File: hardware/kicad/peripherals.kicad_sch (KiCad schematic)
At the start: 28 parts, among them J301 IT8951 HAT, SW301 PEC11R-4215F-S0024, SW302 POWER, U301 CAP1188-1-CP-TR

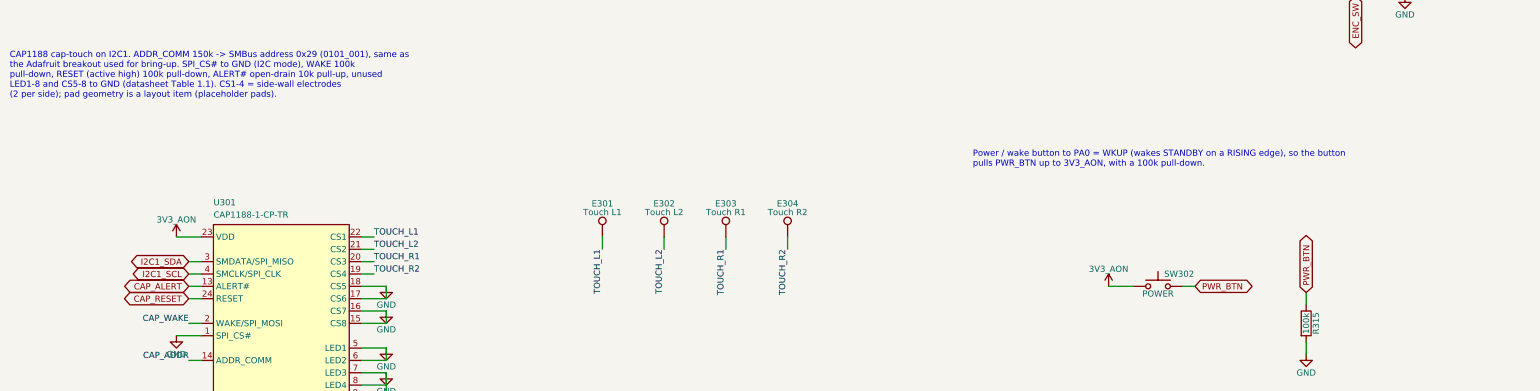
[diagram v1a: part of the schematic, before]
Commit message: Apply enclosure decisions: bottom-edge power button, electrode boards, leaded NTC
Decisions (2026-09-23): keep the HAT's 2x20 header for v1; move the power
button to the bottom edge; put the side-wall electrodes on two small
boards; keep the front-face knob; put RT1 on leads to the cell.

Schematic (via the generator scripts, check_schematic.py passes):
- SW302: Alps SKRTLAE010 side-actuated switch on the PCB's bottom edge.
- E301-E304 test pads -> J302/J303 JST-SH 3-pin (touch / GND / touch),
  cabled to the electrode boards.
- RT1: leaded Murata NXFT15XH103FA2B (same 10k/B3380 curve) on solder
  pads, head taped to the pouch.

Enclosure: flexure tab in the bottom wall over the switch; two identical
74 x 10 mm electrode boards in printed channels on the side walls; PCB
and battery 2.5 mm in from the walls to make room; new checks for the
button travel and electrode coverage (21 pass, no interferences);
electrode_board.json export and a bottom-edge render.

Co-Authored-By: Claude Opus 5.5 <noreply@anthropic.com>
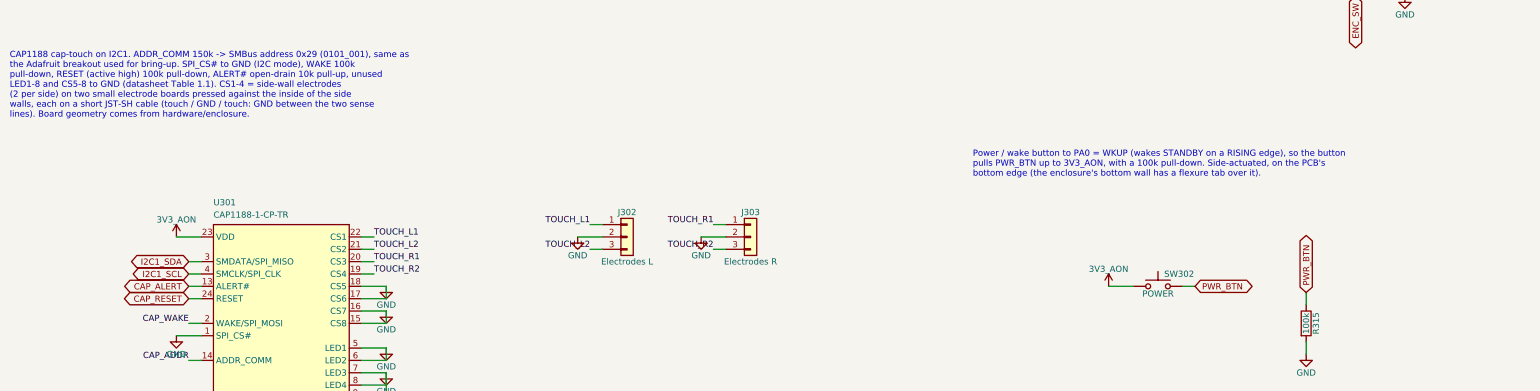
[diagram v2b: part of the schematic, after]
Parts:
- removed E302: Touch L2, TestPoint:TestPoint_Pad_4.0x4.0mm, symbol Connector:TestPoint
- removed E303: Touch R1, TestPoint:TestPoint_Pad_4.0x4.0mm, symbol Connector:TestPoint
- removed E304: Touch R2, TestPoint:TestPoint_Pad_4.0x4.0mm, symbol Connector:TestPoint
- added J303: Electrodes R, Connector_JST:JST_SH_SM03B-SRSS-TB_1x03-1MP_P1.00mm_Horizontal, symbol Connector_Generic:Conn_01x03
- J302: renamed from E301; value Touch L1 -> Electrodes L; footprint TestPoint:TestPoint_Pad_4.0x4.0mm -> Connector_JST:JST_SH_SM03B-SRSS-TB_1x03-1MP_P1.00mm_Horizontal; symbol Connector:TestPoint -> Connector_Generic:Conn_01x03; MPN (none) -> SM03B-SRSS-TB
- SW302: footprint Button_Switch_SMD:SW_Push_1P1T_NO_CK_KMR2 -> Button_Switch_SMD:SW_Push_1P1T-MP_NO_Horizontal_Alps_SKRTLAE010; MPN (none) -> SKRTLAE010
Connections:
- net GND: now also J302.2 (Pin_2), J303.2 (Pin_2)
- net TOUCH_L2: now also J302.3 (Pin_3)
- net TOUCH_R1: now also J303.1 (Pin_1)
- net TOUCH_R2: now also J303.3 (Pin_3)
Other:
- note added: "CAP1188 cap-touch on I2C1. ADDR_COMM 150k -> SMBus address 0x29 (0101_001), same as the Adafruit breakout used for bring-up. SPI_CS# to GND (I2C mode), WAKE 100k pull-down, RESET (active high) 100k pull-down, ALERT# open-drain 10k pull-up, unused LED1-8 and CS5-8 to GND (datasheet Table 1.1). CS1-4 = side-wall electrodes (2 per side) on two small electrode boards pressed against the inside of the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"
- note added: "Power / wake button to PA0 = WKUP (wakes STANDBY on a RISING edge), so the button pulls PWR_BTN up to 3V3_AON, with a 100k pull-down. Side-actuated, on the PCB's bottom edge (the enclosure's bottom wall has a flexure tab over it)."
- note removed: "CAP1188 cap-touch on I2C1. ADDR_COMM 150k -> SMBus address 0x29 (0101_001), same as the Adafruit breakout used for bring-up. SPI_CS# to GND (I2C mode), WAKE 100k pull-down, RESET (active high) 100k pull-down, ALERT# open-drain 10k pull-up, unused LED1-8 and CS5-8 to GND (datasheet Table 1.1). CS1-4 = side-wall electrodes (2 per side); pad geometry is a layout item (placeholder pads)."
- note removed: "Power / wake button to PA0 = WKUP (wakes STANDBY on a RISING edge), so the button pulls PWR_BTN up to 3V3_AON, with a 100k pull-down."

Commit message: Electrode board project, open hardware TODOs, main PCB bootstrap
- hardware/electrode/: side-wall electrode board (one design, two fitted),
  generated by gen_electrode.py (schematic, pad footprint) and
  gen_electrode_pcb.py (board, via KiCad's pcbnew Python) from the
  enclosure's params.py. ERC/DRC/parity clean.
- Datasheet values replace most enclosure placeholders. The encoder is now
  PEC11R-4220F-S0024 (20 mm shaft): the M7 bushing left the 15 mm shaft
  too short for the knob. Knob redesigned around the bushing.
- Schematic: TPD4E05U06 ESD on the electrode lines, HRDY 100k pull-down,
  crystals chosen (NX3225GD 8 MHz / NX3215SA 32.768 kHz) with recomputed
  load caps, all inductors DFE201612E, M2 mounting holes.
- Decisions recorded: USB shield to GND, UVLO restart analysis, soft power
  = STANDBY + WKUP, no fuel gauge on v1, TPS63900 footprint verified.
- Encoder footprint: silkscreen no longer crosses its own lug pads.
- hardware/kicad/stm32-epaper.kicad_pcb: 4-layer board bootstrapped by
  gen_main_pcb.py with the enclosure outline, all footprints and nets, and
  the enclosure-fixed parts placed.

Co-Authored-By: Claude Opus 5.5 <noreply@anthropic.com>
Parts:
- added H301, H302, H303, H304: M2, MountingHole:MountingHole_2.2mm_M2, symbol Mechanical:MountingHole
- added U301: CAP1188-1-CP-TR, Package_DFN_QFN:QFN-24-1EP_4x4mm_P0.5mm_EP2.5x2.5mm, symbol epaper:CAP1188
- added U302: TPD4E05U06DQAR, Package_SON:USON-10_2.5x1.0mm_P0.5mm, symbol Power_Protection:TPD4E05U06DQA
- R316: renamed from U301; value CAP1188-1-CP-TR -> 100k; footprint Package_DFN_QFN:QFN-24-1EP_4x4mm_P0.5mm_EP2.5x2.5mm -> Resistor_SMD:R_0402_1005Metric; symbol epaper:CAP1188 -> Device:R; MPN CAP1188-1-CP-TR -> (none)
- SW301: value PEC11R-4215F-S0024 -> PEC11R-4220F-S0024; MPN PEC11R-4215F-S0024 -> PEC11R-4220F-S0024
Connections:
- net 3V3_AON: now also U301.23 (VDD); no longer R316.23 (VDD)
- net CAP_ADDR: now also U301.14 (ADDR_COMM); no longer R316.14 (ADDR_COMM)
- net CAP_ALERT: now also U301.13 (ALERT#); no longer R316.13 (ALERT#)
- net CAP_RESET: now also U301.24 (RESET); no longer R316.24 (RESET)
- net CAP_WAKE: now also U301.2 (WAKE/SPI_MOSI); no longer R316.2 (WAKE/SPI_MOSI)
- net EPD_HRDY: now also R316.1
- net GND: now also R316.2, U301.1 (SPI_CS#), U301.10 (LED6), U301.11 (LED7), U301.12 (LED8), U301.15 (CS8), U301.16 (CS7), U301.17 (CS6), U301.18 (CS5), U301.25 (GND), U301.5 (LED1), U301.6 (LED2), U301.7 (LED3), U301.8 (LED4), U301.9 (LED5), U302.3 (GND), U302.8 (GND); no longer R316.1 (SPI_CS#), R316.10 (LED6), R316.11 (LED7), R316.12 (LED8), R316.15 (CS8), R316.16 (CS7), R316.17 (CS6), R316.18 (CS5), R316.25 (GND), R316.5 (LED1), R316.6 (LED2), R316.7 (LED3), R316.8 (LED4), R316.9 (LED5)
- net I2C1_SCL: now also U301.4 (SMCLK/SPI_CLK); no longer R316.4 (SMCLK/SPI_CLK)
- net I2C1_SDA: now also U301.3 (SMDATA/SPI_MISO); no longer R316.3 (SMDATA/SPI_MISO)
- net TOUCH_L1: now also U301.22 (CS1), U302.1 (D1+); no longer R316.22 (CS1)
- net TOUCH_L2: now also U301.21 (CS2), U302.2 (D1-); no longer R316.21 (CS2)
- net TOUCH_R1: now also U301.20 (CS3), U302.4 (D2+); no longer R316.20 (CS3)
- net TOUCH_R2: now also U301.19 (CS4), U302.5 (D2-); no longer R316.19 (CS4)
- no-connect marks 0 -> 4
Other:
- note added: "Bourns PEC11R-4220F-S0024 (24 detents, push switch, 20 mm shaft). Bourns suggested filter per channel: 10k pull-up, 10k series, 10nF to GND -> TIM3 encoder mode (PA6/PA7). Switch: 10k pull-up + 10nF, active low. Mounting lugs to GND (metal shaft ESD path)."
- note added: "Mounting holes: M2 thread-forming screws into standoffs on the back cover. Positions come from hardware/enclosure (out/pcb_placement.json)."
- note added: "R316: HRDY would float while the HAT is unpowered; 100k holds it low (reads "busy"). No ESD on J301: it is an internal cable, never user-accessible."
- note added: "U302: ESD on the electrode cables (the boards sit behind 2.2 mm of PA12, but the back-cover seam is ~0.2 mm from their edge). 0.5 pF/line: negligible next to the pads. NC pins are the flow-through partners of the IO pins (TPD4E05U06 datasheet) - route through."
- note removed: "Bourns PEC11R-4215F-S0024 (24 detents, push switch). Bourns suggested filter per channel: 10k pull-up, 10k series, 10nF to GND -> TIM3 encoder mode (PA6/PA7). Switch: 10k pull-up + 10nF, active low. Mounting lugs to GND (metal shaft ESD path)."

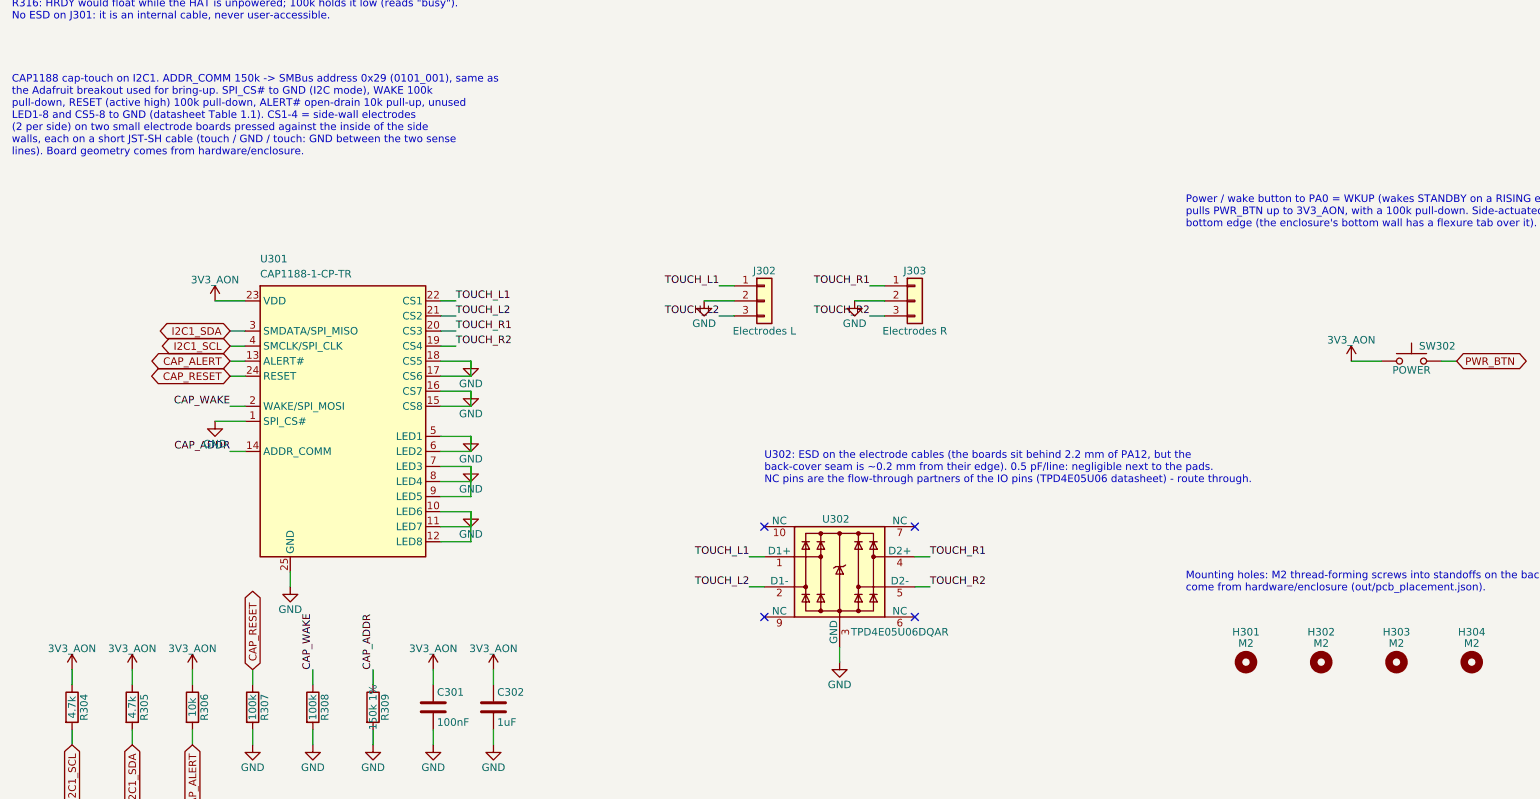
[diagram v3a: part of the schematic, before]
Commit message: Routing attempt 13: 3 unconnected - CAP1188 inputs reassigned, ESD per connector
Left electrodes on CS3/CS4, right on CS5/CS6 (CS1-4 all on the top side
fenced in the VDD pin); U302/U303 TPD2E2U06 right at J302/J303 replace the
single TPD4E05U06.

Co-Authored-By: Claude Opus 5.5 <noreply@anthropic.com>
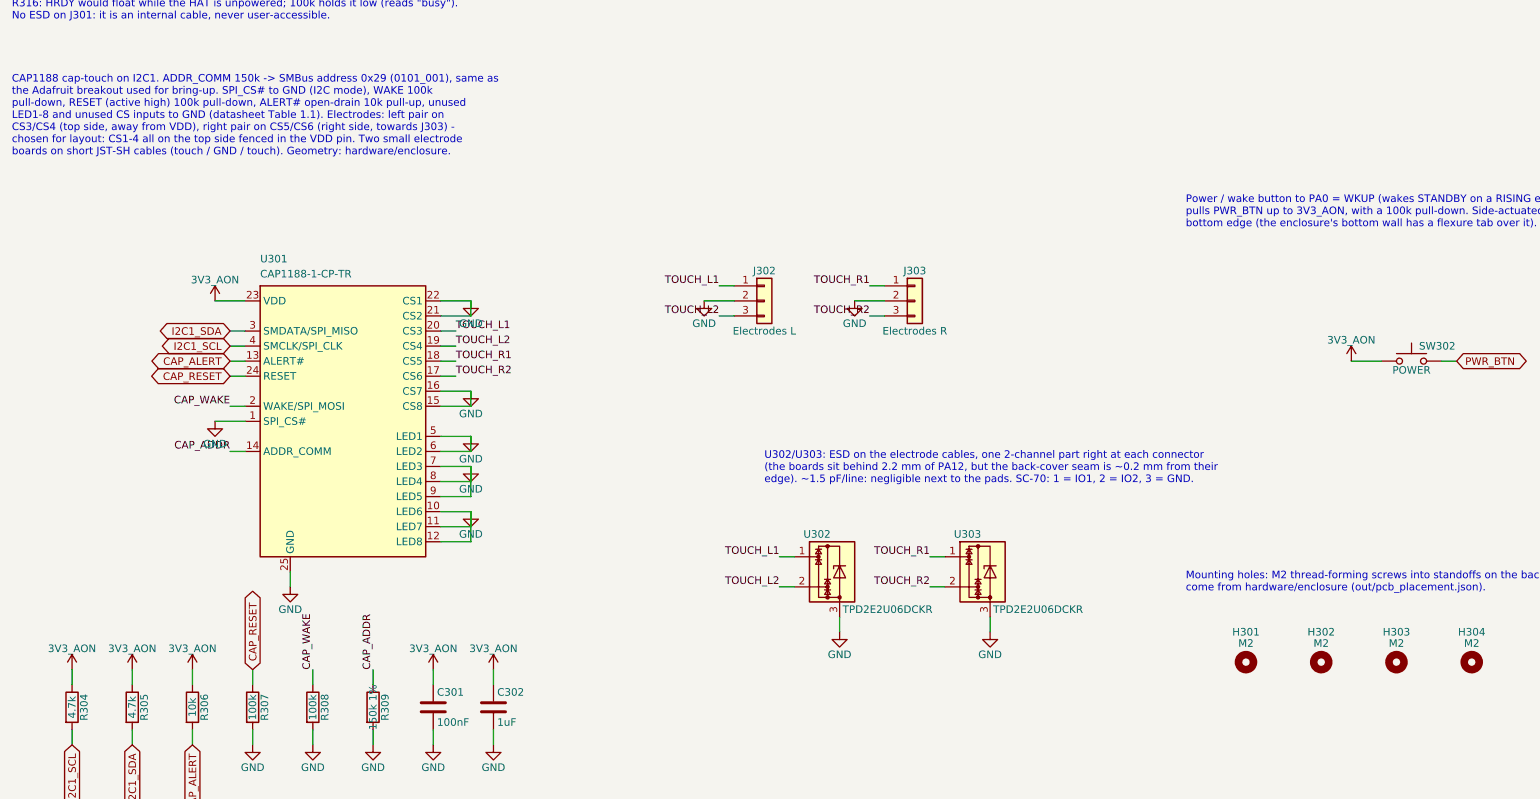
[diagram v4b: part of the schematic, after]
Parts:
- added U303: TPD2E2U06DCKR, Package_TO_SOT_SMD:SOT-323_SC-70, symbol Power_Protection:TPD2E2U06DCK
- U302: value TPD4E05U06DQAR -> TPD2E2U06DCKR; footprint Package_SON:USON-10_2.5x1.0mm_P0.5mm -> Package_TO_SOT_SMD:SOT-323_SC-70; symbol Power_Protection:TPD4E05U06DQA -> Power_Protection:TPD2E2U06DCK; MPN TPD4E05U06DQAR -> TPD2E2U06DCKR
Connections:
- net GND: now also U301.21 (CS2), U301.22 (CS1), U303.3; no longer U301.17 (CS6), U301.18 (CS5), U302.8 (GND)
- net TOUCH_L1: now also U301.20 (CS3); no longer U301.22 (CS1)
- net TOUCH_L2: now also U301.19 (CS4); no longer U301.21 (CS2)
- net TOUCH_R1: now also U301.18 (CS5), U303.1; no longer U301.20 (CS3), U302.4 (D2+)
- net TOUCH_R2: now also U301.17 (CS6), U303.2; no longer U301.19 (CS4), U302.5 (D2-)
- no-connect marks 4 -> 0
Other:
- note added: "CAP1188 cap-touch on I2C1. ADDR_COMM 150k -> SMBus address 0x29 (0101_001), same as the Adafruit breakout used for bring-up. SPI_CS# to GND (I2C mode), WAKE 100k pull-down, RESET (active high) 100k pull-down, ALERT# open-drain 10k pull-up, unused LED1-8 and unused CS inputs to GND (datasheet Table 1.1). Electrodes: left pair on CS3/CS4 (top side, away from VDD), right pair on CS5/CS6 (right side,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"
- note added: "U302/U303: ESD on the electrode cables, one 2-channel part right at each connector (the boards sit behind 2.2 mm of PA12, but the back-cover seam is ~0.2 mm from their edge). ~1.5 pF/line: negligible next to the pads. SC-70: 1 = IO1, 2 = IO2, 3 = GND."
- note removed: "CAP1188 cap-touch on I2C1. ADDR_COMM 150k -> SMBus address 0x29 (0101_001), same as the Adafruit breakout used for bring-up. SPI_CS# to GND (I2C mode), WAKE 100k pull-down, RESET (active high) 100k pull-down, ALERT# open-drain 10k pull-up, unused LED1-8 and CS5-8 to GND (datasheet Table 1.1). CS1-4 = side-wall electrodes (2 per side) on two small electrode boards pressed against the inside of the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"
- note removed: "U302: ESD on the electrode cables (the boards sit behind 2.2 mm of PA12, but the back-cover seam is ~0.2 mm from their edge). 0.5 pF/line: negligible next to the pads. NC pins are the flow-through partners of the IO pins (TPD4E05U06 datasheet) - route through."

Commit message: Board: Michael's routing in KiCad (0 unconnected); schematic pilot: I2C pull-ups wired on the MCU sheet
- stm32-epaper.kicad_pcb as saved from KiCad 2026-09-24 07:39 (last two
  connections routed by hand: DRC 0 unconnected), footprints re-linked to the
  redrawn schematic (R304/R305 -> R105/R106) by sync_board_to_schematic.py.
- Schematic pilot: I2C1 pull-ups drawn wired to PB8/PB9 with junctions
  (moved from the Peripherals sheet). compare_netlists.py: electrically
  identical (156 parts, 193 nets).

Co-Authored-By: Claude Opus 5.5 <noreply@anthropic.com>
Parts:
- removed C301: 100nF, Capacitor_SMD:C_0402_1005Metric, symbol Device:C
- removed C305: 10nF, Capacitor_SMD:C_0402_1005Metric, symbol Device:C
- removed R309: 150k 1%, Resistor_SMD:R_0402_1005Metric, symbol Device:R
- removed R313: 10k, Resistor_SMD:R_0402_1005Metric, symbol Device:R
- added C303, C304: 10nF, Capacitor_SMD:C_0402_1005Metric, symbol Device:C
- C301: renamed from R308; value 100k -> 100nF; footprint Resistor_SMD:R_0402_1005Metric -> Capacitor_SMD:C_0402_1005Metric; symbol Device:R -> Device:C
- R306: renamed from R304; value 4.7k -> 10k
- R307: renamed from R305; value 4.7k -> 100k
- R308: renamed from R306; value 10k -> 100k
- R309: renamed from R307; value 100k -> 150k 1%
- R313: renamed from C303; value 10nF -> 10k; footprint Capacitor_SMD:C_0402_1005Metric -> Resistor_SMD:R_0402_1005Metric; symbol Device:C -> Device:R
- renumbered C304 to C305
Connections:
- net 3V3_AON: now also C301.1; no longer R307.1, R308.1
- net CAP_ADDR: now also R309.1
- net CAP_ALERT: now also R306.2; no longer R308.2
- net CAP_RESET: now also R307.1; no longer R309.1
- net CAP_WAKE: now also R308.1; no longer C301.1
- net ENC_A: now also C303.1; no longer R313.1
- net ENC_B: now also R313.2, C304.1; no longer C305.1
- net ENC_B_RAW: now also R313.1
- net ENC_SW: now also C305.1
- net GND: now also R307.2, R308.2, C303.2, C304.2; no longer R313.2
- net I2C1_SCL: no longer R306.2
- net I2C1_SDA: no longer R307.2
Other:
- moved on the sheet: C305, R306, R307, R308, R309
